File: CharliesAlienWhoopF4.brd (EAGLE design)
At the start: 29 x 29 mm, 41 parts, among them M1 53047-0210, M2 53047-0210, M3 53047-0210, M4 53047-0210, Q1 FDMA410NZ, Q2 FDMA410NZ, Q3 IRLML6402, Q4 FDMA410NZ, Q5 FDMA410NZ, U1 MPU-9250, U2 TPS63001, Y1 8mhz

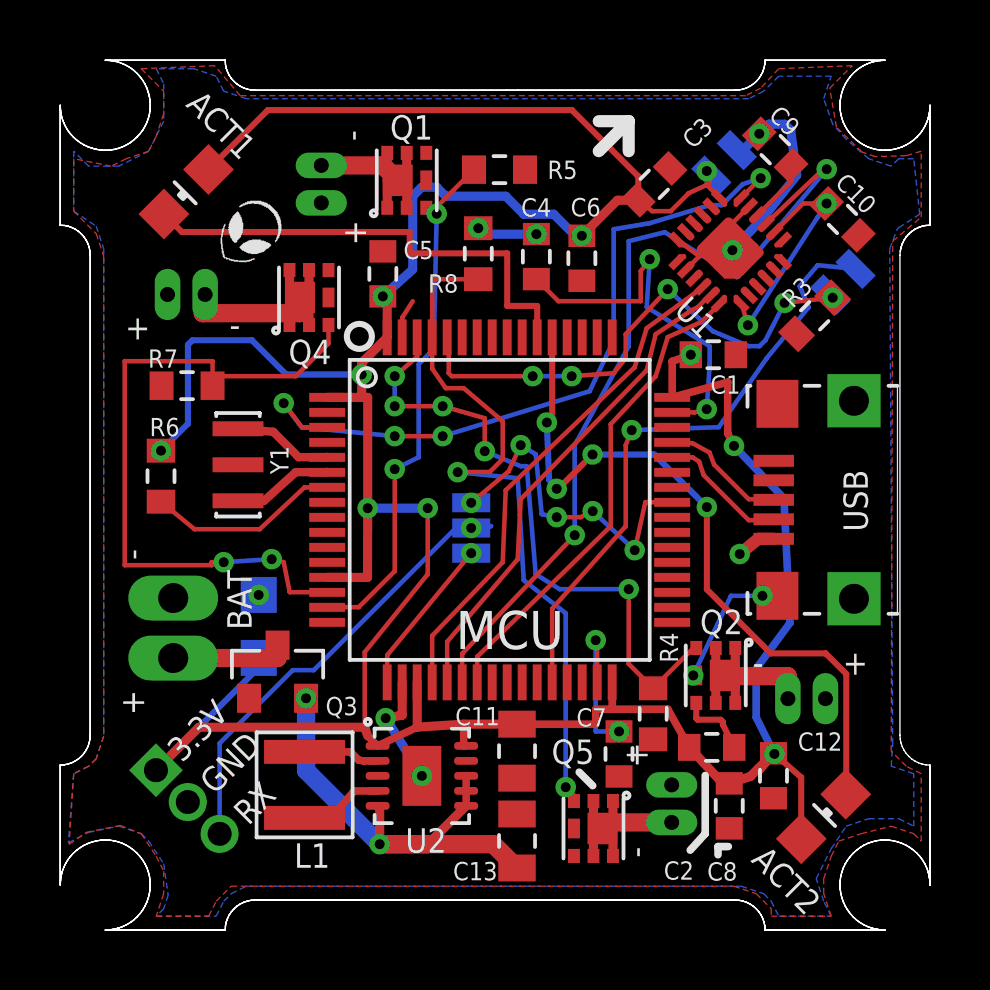
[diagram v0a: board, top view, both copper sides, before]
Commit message: Removed duplicate board outline. Hopefully I got all the line segments. The second run of prototype boards from OSH park it appeared the cut was processed wrong or maybe they just used a larger bit than my outline can handle... anyways... cleaned up. :)
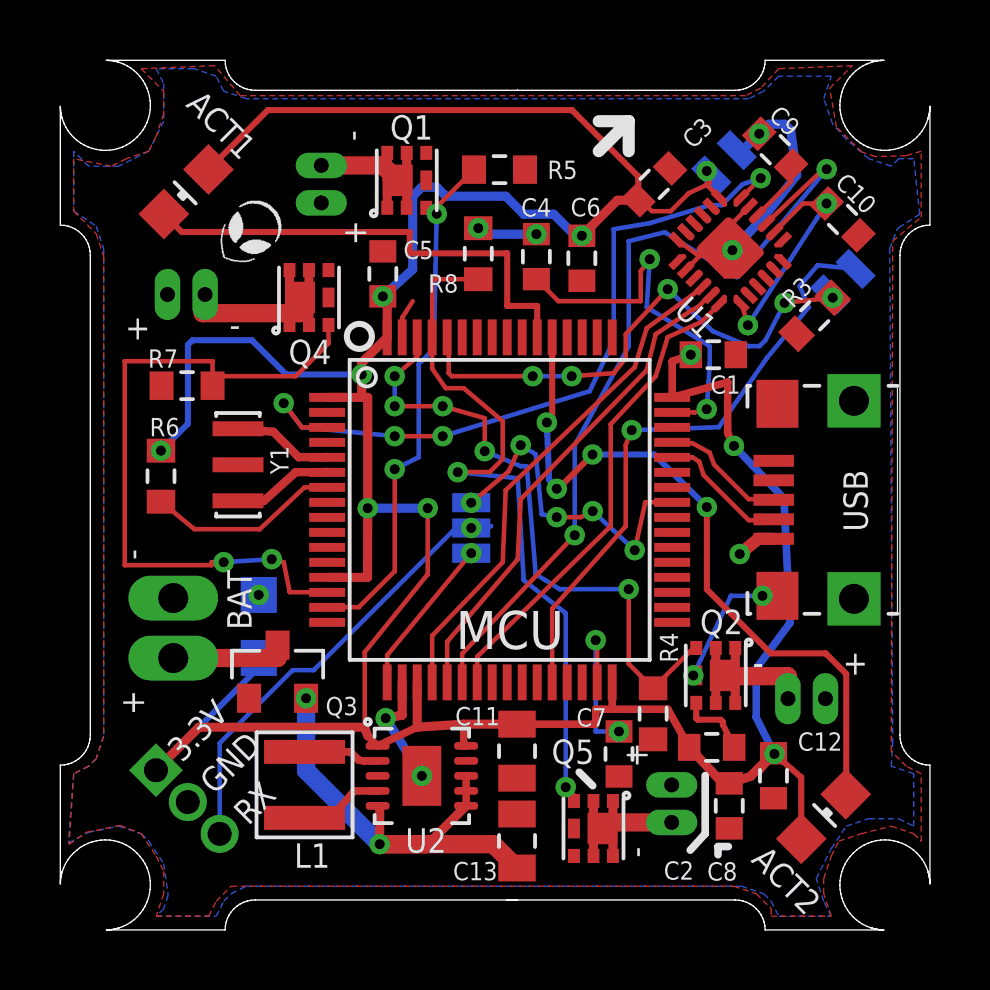
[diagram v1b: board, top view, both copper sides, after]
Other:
- outline, holes or cut-outs redrawn
